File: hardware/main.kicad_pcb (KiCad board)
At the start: 4 copper layers, 84 x 50 mm, 190 parts, among them J1 RJ45-B-1*4, J2 TYPE-C-31-M-12, J3 98424-G52-06ALF, J4 batt, SW1 SK-12D02-G040, U1 RTL8370Nx, U2 AT24C16, U3 IP5306, U4 MC34063AD, U5 MT3420B, U6 MT3420B, Y1 SX3B25.000F1510F30

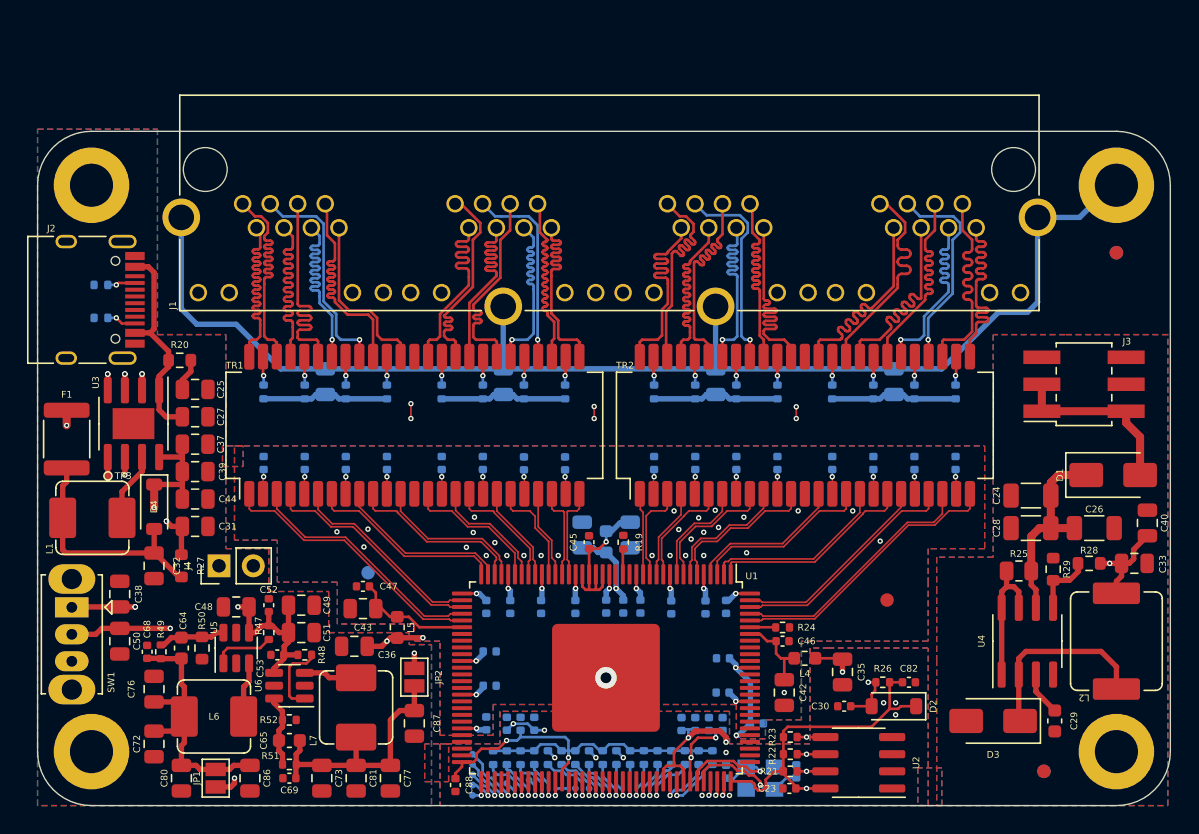
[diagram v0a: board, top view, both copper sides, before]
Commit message: add vias
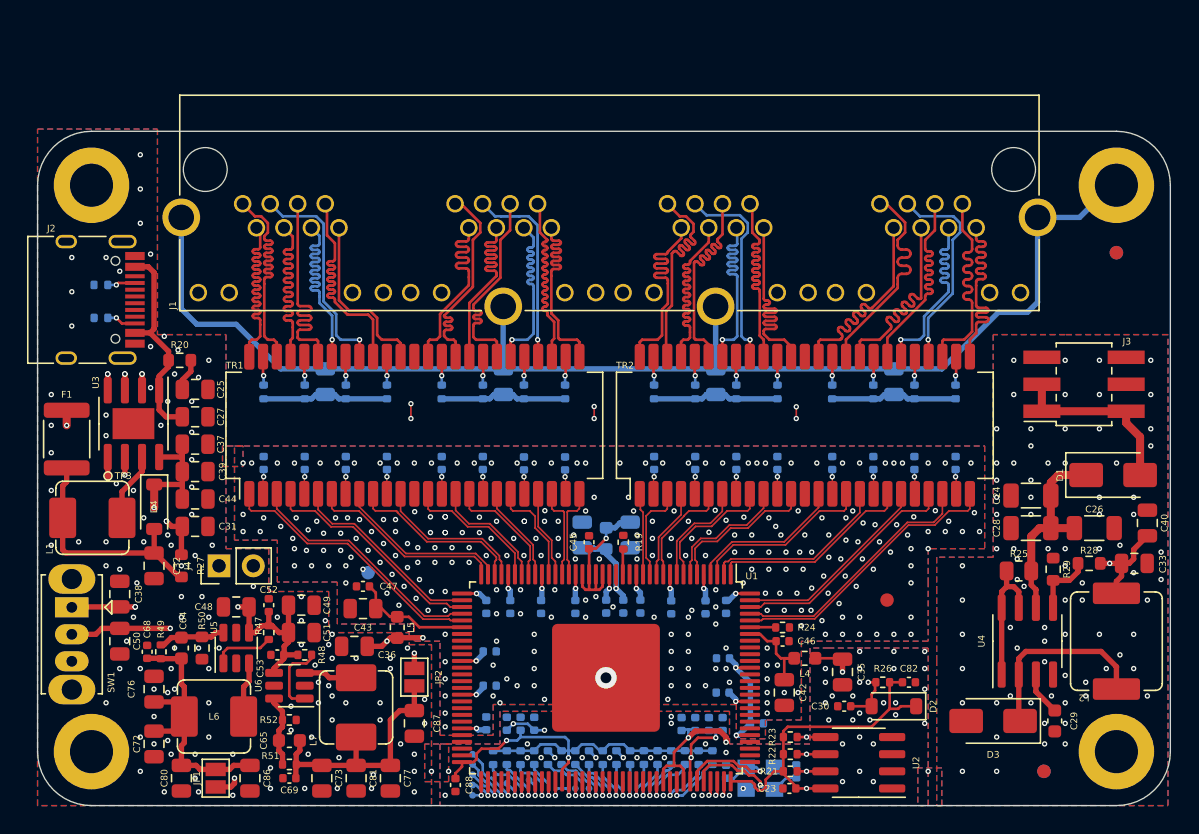
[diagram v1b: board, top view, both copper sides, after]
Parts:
- moved L3 0.25 mm to (42.2, -19.8)
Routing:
- net GND: vias 39 -> 511

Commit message: fix wire
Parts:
- moved FID6 38.5 mm to (63.0, -15.2)
- moved C85 0.85 mm to (53.0, -5.33)
- moved C58 0.62 mm to (44.2, -15.1)
- moved C54 0.52 mm to (33.0, -8.76)
- moved C55 0.52 mm to (33.0, -11.3)
- moved C89 0.46 mm to (51.3, -15.1)
- moved C90 0.46 mm to (33.0, -15.1)
- moved C79 0.43 mm to (43.2, -15.1)
- moved C67 0.43 mm to (46.9, -15.1)
- moved C74 0.43 mm to (49.4, -15.1)
- moved C66 0.40 mm to (34.9, -15.1)
- moved C56 0.38 mm to (39.9, -15.1)
- moved C61 0.38 mm to (37.3, -15.1)
- moved C78 0.38 mm to (51.2, -8.38)
- moved C70 0.35 mm to (42.2, -15.1)
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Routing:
- net Net-(TR2A-TD4+): track 8.94 -> 12.0 mm
- net +1V1: track 163.6 -> 161.1 mm
- net +3V3: track 161.4 -> 158.9 mm
- net Net-(TR2B-TD3+): track 15.1 -> 17.3 mm
- net Net-(TR1A-TD2-): track 14.6 -> 16.8 mm
- net Net-(TR1A-TD1-): track 18.2 -> 20.3 mm
- net Net-(TR2B-TD4+): track 19.0 -> 20.8 mm
- net Net-(TR2A-TD3+): track 7.36 -> 9.14 mm
- net Net-(TR1B-TD2-): track 7.14 -> 8.90 mm
- net Net-(TR1A-TD3-): track 12.9 -> 14.6 mm
- net Net-(TR2B-TD1+): track 11.6 -> 13.2 mm
- net Net-(TR1B-TD1-): track 8.90 -> 10.4 mm
- net Net-(TR2A-TD2+): track 6.02 -> 7.46 mm
- net Net-(TR1A-TD4-): track 11.4 -> 12.9 mm
- net Net-(TR2B-TD2+): track 13.9 -> 15.1 mm
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
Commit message: fix pcb and check drc
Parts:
- added R53: 470R, Resistor_SMD:R_0402_1005Metric, B.Cu at (45.7, -44.8)
- added R54: 470R, Resistor_SMD:R_0402_1005Metric, B.Cu at (30.0, -44.8)
- added R55: 470R, Resistor_SMD:R_0402_1005Metric, B.Cu at (14.2, -44.8)
- added TP11: TestPoint, MAS_Package_std:TestPoint_Pad_D0.5mm, F.Cu at (33.4, -2.59)
- C21, C22, L3, R30, R31, R33, R34, R35, R36, R37, R38, R39, R40, R41, R42, R43, R44, R45, R46, TP1, TP10, TP2, TP4, TP5, TP6, TP7, TP8, TP9, Y1: moved to F.Cu
- C88: moved to B.Cu
- R32: value 4.7k -> 470R
- moved FID1 64.6 mm to (10.0, -3.00)
- moved FID4 64.6 mm to (10.0, -3.00)
- moved R32 48.6 mm to (61.5, -44.8)
- moved FID3 15.7 mm to (74.0, -4.00)
- moved FID6 15.7 mm to (74.0, -4.00)
- moved C88 7.31 mm to (33.5, -8.38), turned to 0 degrees
- moved TP1 6.66 mm to (31.4, -7.37), turned to 180 degrees
- moved C45 5.87 mm to (40.9, -25.4)
- moved R19 5.87 mm to (43.4, -25.4)
- moved C85 5.86 mm to (51.2, -10.9), turned to 180 degrees
- moved C21 5.51 mm to (51.3, -4.95), turned to 0 degrees
- moved TP3 5.19 mm to (4.57, -29.6)
- moved TP2 5.16 mm to (31.4, -6.60), turned to 180 degrees
- moved C17 5.00 mm to (21.3, -36.4)
- moved C18 5.00 mm to (34.5, -36.4)
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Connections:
- R32 pad 1: Net-(U1I-P5LED0) -> /G4+
- R34 pad 1: Net-(U1I-P4LED0/SLED_P6B/STRP_EEPROM_MOD) -> /G2-
- R37 pad 1: Net-(U1I-P3LED0/SLED_P2B/STRP_EN_FLASH) -> /G3-
- R39 pad 1: Net-(U1I-P2LED0/SLED_P0B/STRP_DISAUTOLOAD) -> /G4-
- U1 pad 103: (no net) -> unconnected-(U1A-P0MDIAP-Pad103)
- U1 pad 104: (no net) -> unconnected-(U1A-P0MDIAN-Pad104)
- U1 pad 105: (no net) -> unconnected-(U1A-P0MDIBP-Pad105)
- U1 pad 106: (no net) -> unconnected-(U1A-P0MDIBN-Pad106)
- U1 pad 108: (no net) -> unconnected-(U1A-P0MDICP-Pad108)
- U1 pad 109: (no net) -> unconnected-(U1A-P0MDICN-Pad109)
- U1 pad 110: (no net) -> unconnected-(U1A-P0MDIDP-Pad110)
- U1 pad 111: (no net) -> unconnected-(U1A-P0MDIDN-Pad111)
- U1 pad 113: (no net) -> unconnected-(U1B-P1MDIAP-Pad113)
- U1 pad 114: (no net) -> unconnected-(U1B-P1MDIAN-Pad114)
- U1 pad 115: (no net) -> unconnected-(U1B-P1MDIBP-Pad115)
- U1 pad 116: (no net) -> unconnected-(U1B-P1MDIBN-Pad116)
- U1 pad 118: (no net) -> unconnected-(U1B-P1MDICP-Pad118)
- U1 pad 119: (no net) -> unconnected-(U1B-P1MDICN-Pad119)
- U1 pad 120: (no net) -> unconnected-(U1B-P1MDIDP-Pad120)
- U1 pad 121: (no net) -> unconnected-(U1B-P1MDIDN-Pad121)
- U1 pad 74: Net-(U1I-P5LED0) -> /G1-
- U1 pad 80: Net-(U1I-P4LED0/SLED_P6B/STRP_EEPROM_MOD) -> /G2-
- U1 pad 84: Net-(U1I-P3LED0/SLED_P2B/STRP_EN_FLASH) -> /G3-
- U1 pad 86: Net-(U1I-P2LED0/SLED_P0B/STRP_DISAUTOLOAD) -> /G4-
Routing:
- net +3V3: track 158.9 -> 256.2 mm, vias 13 -> 18
- net /G1-: track 0.00 -> 75.3 mm, vias 0 -> 2
- net /G2-: track 0.00 -> 60.5 mm, vias 0 -> 2
- net /G4-: track 0.00 -> 59.2 mm, vias 0 -> 2
- net /G3-: track 0.00 -> 46.3 mm, vias 0 -> 2
- net +1V1: track 161.1 -> 155.7 mm
- net Net-(U1I-P4LED0/SLED_P6B/STRP_EEPROM_MOD): track 5.10 -> 0.00 mm, vias 1 -> 0
- net Net-(U1I-P5LED0): track 4.42 -> 0.00 mm, vias 1 -> 0
- net Net-(U1I-P3LED0/SLED_P2B/STRP_EN_FLASH): track 4.15 -> 0.00 mm, vias 1 -> 0
- net Net-(U1I-P2LED0/SLED_P0B/STRP_DISAUTOLOAD): track 3.54 -> 0.00 mm, vias 1 -> 0
- net Net-(U1I-P6LED2/nSPI_F_CS): track 2.20 -> 5.72 mm, vias 1 -> 0
- net Net-(U1I-P3LED2/SLED_P3B/STRP_EN_PWRLIGHT): track 4.36 -> 7.58 mm
- net Net-(U1I-P3LED1/SLED_G1A/GPIO5): track 4.92 -> 8.14 mm
- net Net-(D2-A): track 21.4 -> 18.5 mm
- net Net-(U1I-P6LED1/GPIO7): track 4.11 -> 7.02 mm
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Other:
- board size 84 x 50 mm -> 84 x 55 mm

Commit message: fix wire
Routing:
- net Net-(J1A-BI_DC-): track 17.7 -> 12.7 mm
- net Net-(J1C-BI_DD+): track 16.7 -> 11.8 mm
- net Net-(J1A-BI_DC+): track 17.7 -> 12.8 mm
- net Net-(J1C-BI_DD-): track 16.5 -> 11.7 mm
- net Net-(J1A-BI_DA+): track 17.7 -> 13.1 mm
- net Net-(J1A-BI_DA-): track 17.7 -> 13.2 mm
- net Net-(J1D-BI_DD-): track 16.8 -> 12.4 mm
- net Net-(J1D-BI_DD+): track 16.8 -> 12.6 mm
- net Net-(J1A-BI_DD+): track 17.8 -> 13.7 mm
- net Net-(J1D-BI_DC+): track 16.7 -> 12.7 mm
- net Net-(J1D-BI_DC-): track 16.7 -> 12.8 mm
- net Net-(J1B-BI_DD-): track 15.6 -> 11.8 mm
- net Net-(J1B-BI_DD+): track 15.7 -> 11.9 mm
- net Net-(J1C-BI_DC-): track 16.7 -> 13.0 mm
- net Net-(J1C-BI_DC+): track 16.4 -> 13.0 mm
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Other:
- board text added: "JLCJLCJLCJLC"
- board text added: "OPS"
- board text added: "Open pocket switch"
- board text added: "rev 0.1"

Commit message: completion of development.
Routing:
- net Net-(TR2A-TD3+): track 9.14 -> 6.11 mm
